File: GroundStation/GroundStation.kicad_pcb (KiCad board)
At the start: 2 copper layers, 57.1 x 50 mm, 10 parts, among them P1 CONN_01X02, U1 ARDUPROMINI, U2 RFM95, U3 LM2596_DC-DC

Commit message: Fix Ground station <3
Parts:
- added P2: ADJ, Pin_Headers:Pin_Header_Straight_1x02, F.Cu at (114.8, 78.9)
- D1, D2: value D -> 1N400x
- G***: moved to F.Cu
- moved G*** 15.8 mm to (148.8, 109.3), turned to 0 degrees
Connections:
- U3 pad 1: Net-(D1-Pad1) -> Net-(P2-Pad2)
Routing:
- net Net-(D1-Pad1): track 25.4 -> 19.0 mm
- net Net-(P2-Pad2): track 0.00 -> 3.88 mm
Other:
- board text added: "CatSat 1.1v"
- board text added: "Ground Station"
- board text removed: "CatSat I"
- board text removed: "Earth Station"

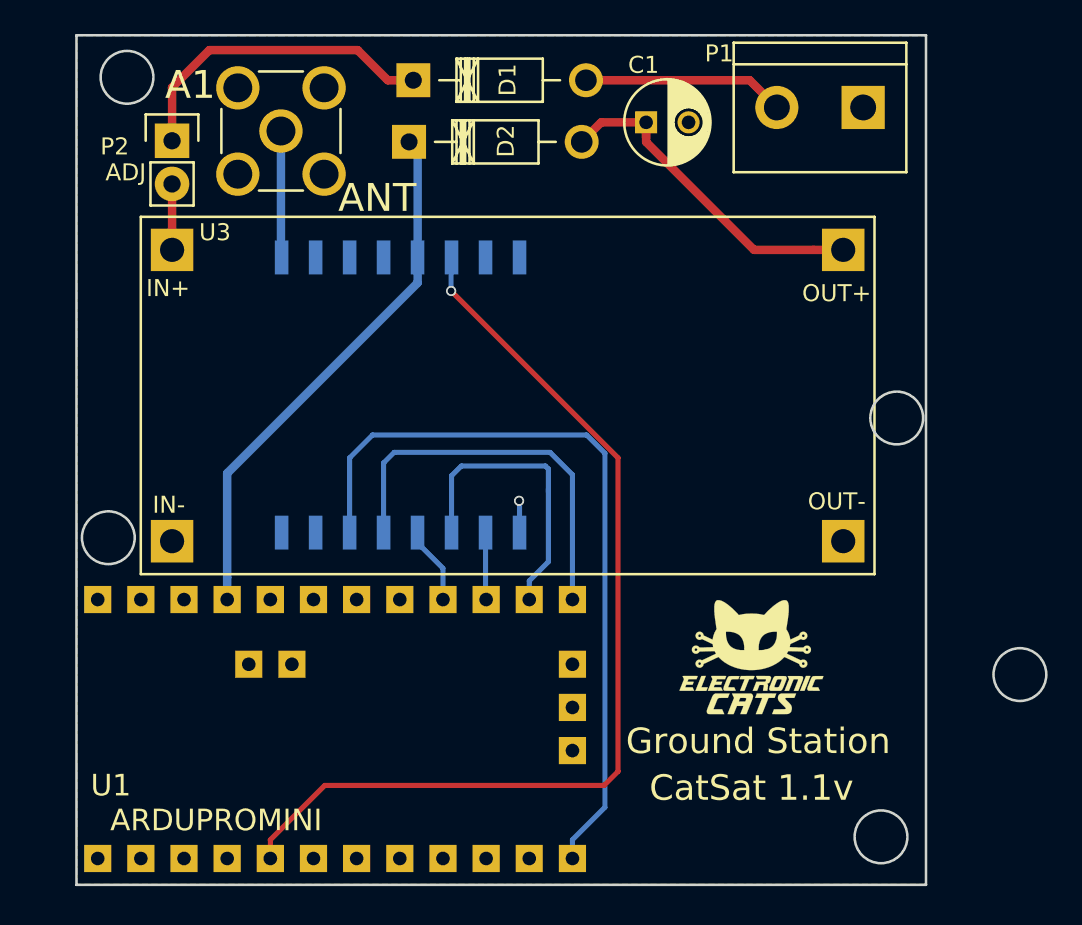
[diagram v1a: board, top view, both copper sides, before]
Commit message: Add extra I/O pins Ground station
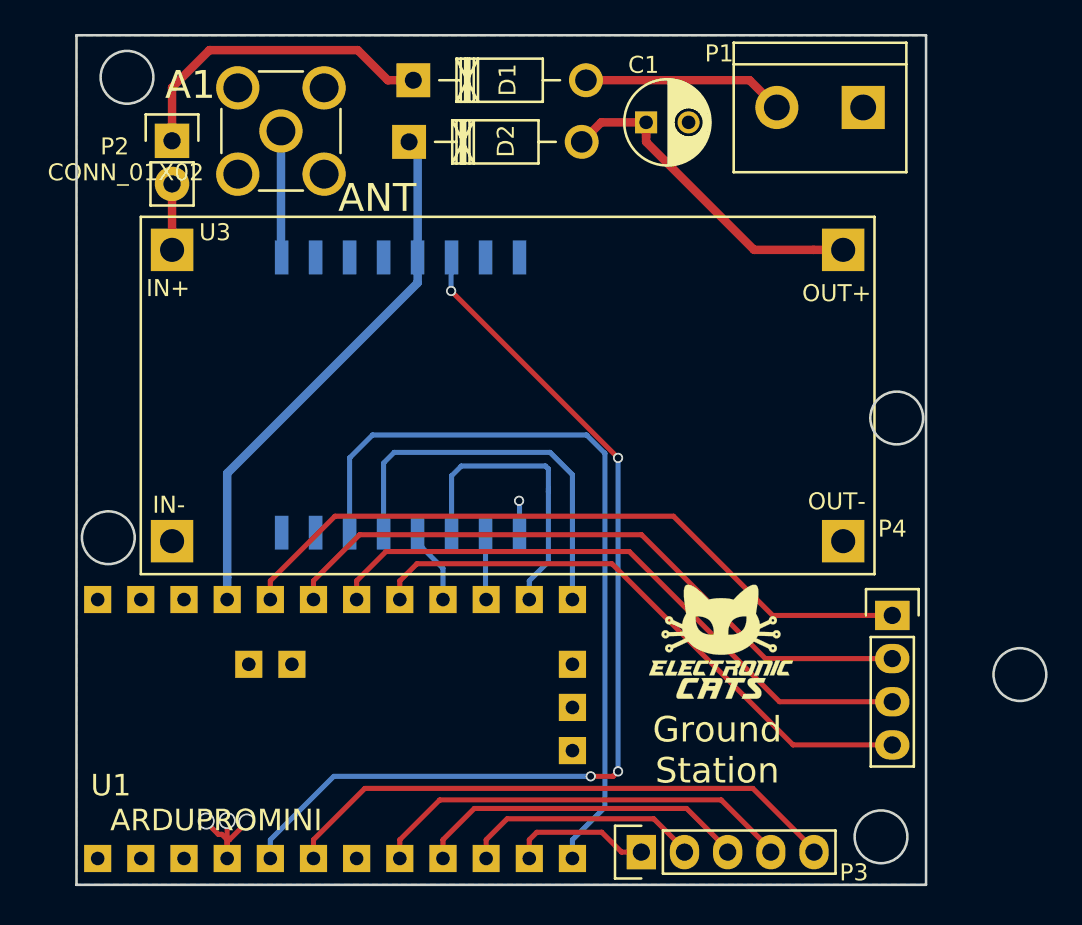
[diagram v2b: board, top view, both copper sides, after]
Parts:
- added P3: CONN_01X05, Pin_Headers:Pin_Header_Straight_1x05, F.Cu at (142.4, 120.8)
- added P4: CONN_01X04, Pin_Headers:Pin_Header_Straight_1x04, F.Cu at (157.1, 106.8)
- D2: value 1N400x -> D
- P2: value ADJ -> CONN_01X02
- moved REF** 19.9 mm to (145.2, 71.7)
- moved G*** 2.01 mm to (147.1, 108.4)
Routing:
- net Net-(P4-Pad1): track 0.00 -> 41.7 mm
- net Net-(P4-Pad2): track 0.00 -> 39.3 mm
- net Net-(P4-Pad3): track 0.00 -> 37.0 mm
- net Net-(P4-Pad4): track 0.00 -> 34.9 mm
- net Net-(P3-Pad5): track 0.00 -> 33.5 mm
- net Net-(P3-Pad4): track 0.00 -> 25.3 mm
- net Net-(P3-Pad3): track 0.00 -> 19.8 mm
- net Net-(P3-Pad2): track 0.00 -> 14.2 mm
- net Net-(P3-Pad1): track 0.00 -> 8.36 mm
- net GND: track 2.80 -> 9.46 mm, vias 1 -> 4
- net /INT0: track 58.6 -> 57.6 mm, vias 1 -> 4
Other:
- board text added: "A1 A0"
- board text added: "A3 A2"
- board text added: "D3"
- board text added: "D6 D5"
- board text added: "D8 D7"

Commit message: Fix Labels GroundStation
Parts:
- P2: value CONN_01X02 -> ADJ
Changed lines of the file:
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@@
     (at 116.725 116.045 90)
     (descr ABK-PRO-MINI)
-    (fp_text reference U1 (at -0.78 -5.575 180) (layer F.SilkS)
+    (fp_text reference U1 (at 7.245 -5.525 180) (layer F.SilkS)
       (effects (font (thickness 0.15)))
     )
-    (fp_text value ARDUPROMINI (at -2.83 0.625 360) (layer F.SilkS)
+    (fp_text value ARDUPROMINI (at -0.955 0.875 360) (layer F.SilkS)
       (effects (font (thickness 0.15)))
     )
@@
     (at 121.16 78.31)
     (solder_mask_margin 0.1)
-    (fp_text reference A1 (at -5.34 -2.71) (layer F.SilkS)
+    (fp_text reference A1 (at -5.34 -2.71) (layer F.Fab)
       (effects (font (size 1.64 1.64) (thickness 0.05)))
     )
     (fp_text value ANT (at 5.665 3.94) (layer F.SilkS)
-      (effects (font (size 1.64 1.64) (thickness 0.05)))
+      (effects (font (size 1.64 1.64) (thickness 0.3)))
     )
     (fp_line (start -1.2954 3.5052) (end 1.2954 3.5052) (layer F.SilkS) (width 0.1524))
@@
   (module CatSat:RFM (layer B.Cu)
     (at 128.2 93.85 90)
-    (fp_text reference U2 (at -6.52 9.16 270) (layer B.SilkS)
-      (effects (font (size 0.77216 0.77216) (thickness 0.138988)) (justify left bottom mirror))
-    )
-    (fp_text value RFM95 (at 8.04 8.79 270) (layer B.SilkS)
-      (effects (font (size 0.38608 0.38608) (thickness 0.038608)) (justify left bottom mirror))
+    (fp_text reference U2 (at -5.95 9.6 90) (layer B.SilkS)
+      (effects (font (size 1 1) (thickness 0.25)) (justify left bottom mirror))
+    )
+    (fp_text value RFM95 (at 8.04 9.6 90) (layer B.SilkS)
+      (effects (font (size 1 1) (thickness 0.25)) (justify left bottom mirror))
     )
     (fp_line (start -8 8) (end 8 8) (layer Dwgs.User) (width 0.127))
@@
     (descr "Through hole pin header")
     (tags "pin header")
-    (fp_text reference P2 (at -3.375 0.34) (layer F.SilkS)
-      (effects (font (size 1 1) (thickness 0.15)))
-    )
-    (fp_text value CONN_01X02 (at -2.725 1.865) (layer F.SilkS)
+    (fp_text reference P2 (at 0.25 -2.485) (layer F.SilkS)
+      (effects (font (size 1 1) (thickness 0.15)))
+    )
+    (fp_text value ADJ (at -2.35 0.915 90) (layer F.SilkS)
       (effects (font (size 1 1) (thickness 0.15)))
     )
@@
     (connect_pads (clearance 0.508))
     (min_thickness 0.254)
-    (fill yes (arc_segments 16) (thermal_gap 0.508) (thermal_bridge_width 0.508))
+    (fill (arc_segments 16) (thermal_gap 0.508) (thermal_bridge_width 0.508))
     (polygon
       (pts
@@
     (connect_pads (clearance 0.508))
     (min_thickness 0.254)
-    (fill yes (arc_segments 16) (thermal_gap 0.8) (thermal_bridge_width 0.508))
+    (fill (arc_segments 16) (thermal_gap 0.8) (thermal_bridge_width 0.508))
     (polygon
       (pts
